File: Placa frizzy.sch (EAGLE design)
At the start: 85 parts, among them IC2 LM358D, Q1 2N7002PW, Q4 FDN340P, Q5 FDN340P, U1 FTS31XS-U, U2 AMS1117-3.3, U4 ATMEGA328P_TQFP, Y1 16MHZ

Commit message: Ultima version mandada a fabrica
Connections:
- removed net VCC: C12.1, C13.1, C14.1, JP1.2, JP10.2, JP11.2, JP12.2, JP13.2, JP14.2, JP15.2, JP16.2, JP17.2, JP18.2, JP20.2, JP21.2, JP22.2, JP23.2, JP24.2, JP25.2, JP26.2, JP5.2, JP6.2, JP7.2, JP8.2, JP9.2, R3.2, R8.2, U4.AVCC, U4.VCC@4, U4.VCC@6
- net 5V: now also C12.1, C13.1, C14.1, JP1.2, JP10.2, JP11.2, JP12.2, JP13.2, JP14.2, JP15.2, JP16.2, JP17.2, JP18.2, JP20.2, JP21.2, JP22.2, JP23.2, JP24.2, JP25.2, JP26.2, JP5.2, JP6.2, JP7.2, JP8.2, JP9.2, R3.2, R8.2, U4.AVCC, U4.VCC@4, U4.VCC@6

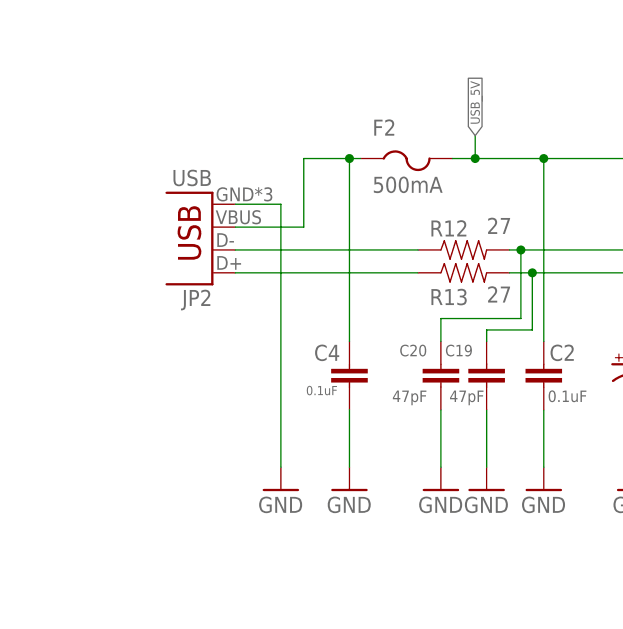
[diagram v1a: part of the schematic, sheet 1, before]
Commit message: Vias Tapadas, USB cambiado, TX RX añadido
se ha reparado tambien la alimentacion de 5V
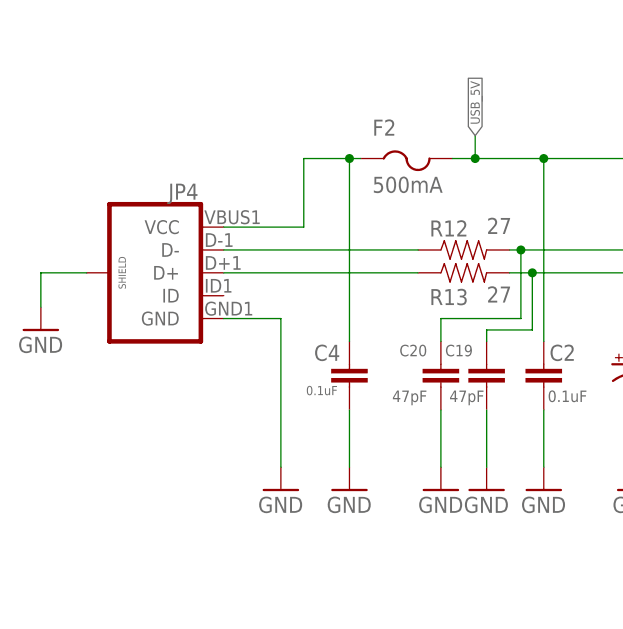
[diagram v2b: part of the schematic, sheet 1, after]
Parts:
- removed JP2: USB, SparkFun-Connectors:USB-MICROB
- added JP4: (no value), SparkFun-Connectors:USB_MICROB_PLUGCONN-11752
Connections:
- net GND: now also JP4.GND, JP4.SHIELD; no longer JP2.GND
- net N$24: now also JP4.D-; no longer JP2.D-
- net N$28: now also JP4.D+; no longer JP2.D+
- net N$29: now also JP4.VCC; no longer JP2.VBUS
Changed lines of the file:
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@@
 <?xml version="1.0" encoding="utf-8"?>
 <!DOCTYPE eagle SYSTEM "eagle.dtd">
-<eagle version="7.3.0">
+<eagle version="7.7.0">
 <drawing>
 <settings>
@@
 <setting verticaltext="up"/>
 </settings>
-<grid distance="0.05" unitdist="inch" unit="inch" style="lines" multiple="1" display="no" altdistance="0.01" altunitdist="inch" altunit="inch"/>
+<grid distance="0.05" unitdist="inch" unit="inch" style="lines" multiple="1" display="yes" altdistance="0.01" altunitdist="inch" altunit="inch"/>
 <layers>
 <layer number="1" name="Top" color="4" fill="1" visible="no" active="no"/>
@@
 <part name="R12" library="SparkFun-Passives" deviceset="RESISTOR" device="0805-RES" value="27"/>
 <part name="R13" library="SparkFun-Passives" deviceset="RESISTOR" device="0805-RES" value="27"/>
-<part name="JP2" library="SparkFun-Connectors" deviceset="USB" device="-MICROB" value="USB"/>
 <part name="GND22" library="SparkFun-Aesthetics" deviceset="GND" device=""/>
 <part name="C19" library="SparkFun-Passives" deviceset="CAP" device="0805" value="47pF"/>
@@
 <part name="SUPPLY40" library="SparkFun-Aesthetics" deviceset="5V" device=""/>
 <part name="SUPPLY41" library="SparkFun-Aesthetics" deviceset="5V" device=""/>
+<part name="JP4" library="SparkFun-Connectors" deviceset="USB_MICROB_PLUG" device="CONN-11752"/>
+<part name="GND10" library="SparkFun-Aesthetics" deviceset="GND" device=""/>
 </parts>
 <sheets>
@@
 <attribute name="VALUE" x="-24.13" y="38.608" size="1.778" layer="96"/>
 </instance>
-<instance part="JP2" gate="G$1" x="-54.61" y="49.53" rot="R180"/>
 <instance part="GND22" gate="1" x="-39.37" y="17.78"/>
 <instance part="C19" gate="G$1" x="-24.13" y="31.75" smashed="yes" rot="R180">
@@
 <instance part="R15" gate="G$1" x="64.77" y="49.53" rot="R270"/>
 <instance part="SUPPLY13" gate="G$1" x="64.77" y="57.15"/>
+<instance part="JP4" gate="G$1" x="-60.96" y="41.91" rot="MR0"/>
+<instance part="GND10" gate="1" x="-73.66" y="35.56"/>
 </instances>
 <busses>
@@
 </segment>
 <segment>
-<pinref part="GND4" gate="1" pin="GND"/>
-<wire x1="-46.99" y1="20.32" x2="-46.99" y2="49.53" width="0.1524" layer="91"/>
-<pinref part="JP2" gate="G$1" pin="GND"/>
-<wire x1="-46.99" y1="49.53" x2="-52.07" y2="49.53" width="0.1524" layer="91"/>
-</segment>
-<segment>
 <pinref part="C4" gate="G$1" pin="2"/>
 <pinref part="GND22" gate="1" pin="GND"/>
@@
 <wire x1="-24.13" y1="26.67" x2="-24.13" y2="20.32" width="0.1524" layer="91"/>
 </segment>
+<segment>
+<pinref part="JP4" gate="G$1" pin="GND"/>
+<pinref part="GND4" gate="1" pin="GND"/>
+<wire x1="-53.34" y1="36.83" x2="-46.99" y2="36.83" width="0.1524" layer="91"/>
+<wire x1="-46.99" y1="36.83" x2="-46.99" y2="20.32" width="0.1524" layer="91"/>
+</segment>
+<segment>
+<pinref part="GND10" gate="1" pin="GND"/>
+<wire x1="-73.66" y1="38.1" x2="-73.66" y2="41.91" width="0.1524" layer="91"/>
+<pinref part="JP4" gate="G$1" pin="SHIELD"/>
+<wire x1="-73.66" y1="41.91" x2="-68.58" y2="41.91" width="0.1524" layer="91"/>
+</segment>
 </net>
 <net name="3.3V" class="0">
@@
 <net name="N$24" class="0">
 <segment>
-<pinref part="JP2" gate="G$1" pin="D-"/>
 <pinref part="R12" gate="G$1" pin="1"/>
-<wire x1="-52.07" y1="44.45" x2="-31.75" y2="44.45" width="0.1524" layer="91"/>
+<wire x1="-53.34" y1="44.45" x2="-31.75" y2="44.45" width="0.1524" layer="91"/>
+<pinref part="JP4" gate="G$1" pin="D-"/>
 </segment>
 </net>
 <net name="N$28" class="0">
 <segment>
-<pinref part="JP2" gate="G$1" pin="D+"/>
 <pinref part="R13" gate="G$1" pin="1"/>
-<wire x1="-52.07" y1="41.91" x2="-31.75" y2="41.91" width="0.1524" layer="91"/>
+<wire x1="-53.34" y1="41.91" x2="-31.75" y2="41.91" width="0.1524" layer="91"/>
+<pinref part="JP4" gate="G$1" pin="D+"/>
 </segment>
 </net>
 <net name="N$29" class="0">
 <segment>
-<pinref part="JP2" gate="G$1" pin="VBUS"/>
-<wire x1="-52.07" y1="46.99" x2="-44.45" y2="46.99" width="0.1524" layer="91"/>
+<wire x1="-53.34" y1="46.99" x2="-44.45" y2="46.99" width="0.1524" layer="91"/>
 <wire x1="-44.45" y1="46.99" x2="-44.45" y2="54.61" width="0.1524" layer="91"/>
 <pinref part="F2" gate="G$1" pin="1"/>
@@
 <wire x1="-39.37" y1="34.29" x2="-39.37" y2="54.61" width="0.1524" layer="91"/>
 <junction x="-39.37" y="54.61"/>
+<pinref part="JP4" gate="G$1" pin="VCC"/>
 </segment>
 </net>
